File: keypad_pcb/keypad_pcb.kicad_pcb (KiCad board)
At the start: 2 copper layers, 40 x 60 mm, 32 parts

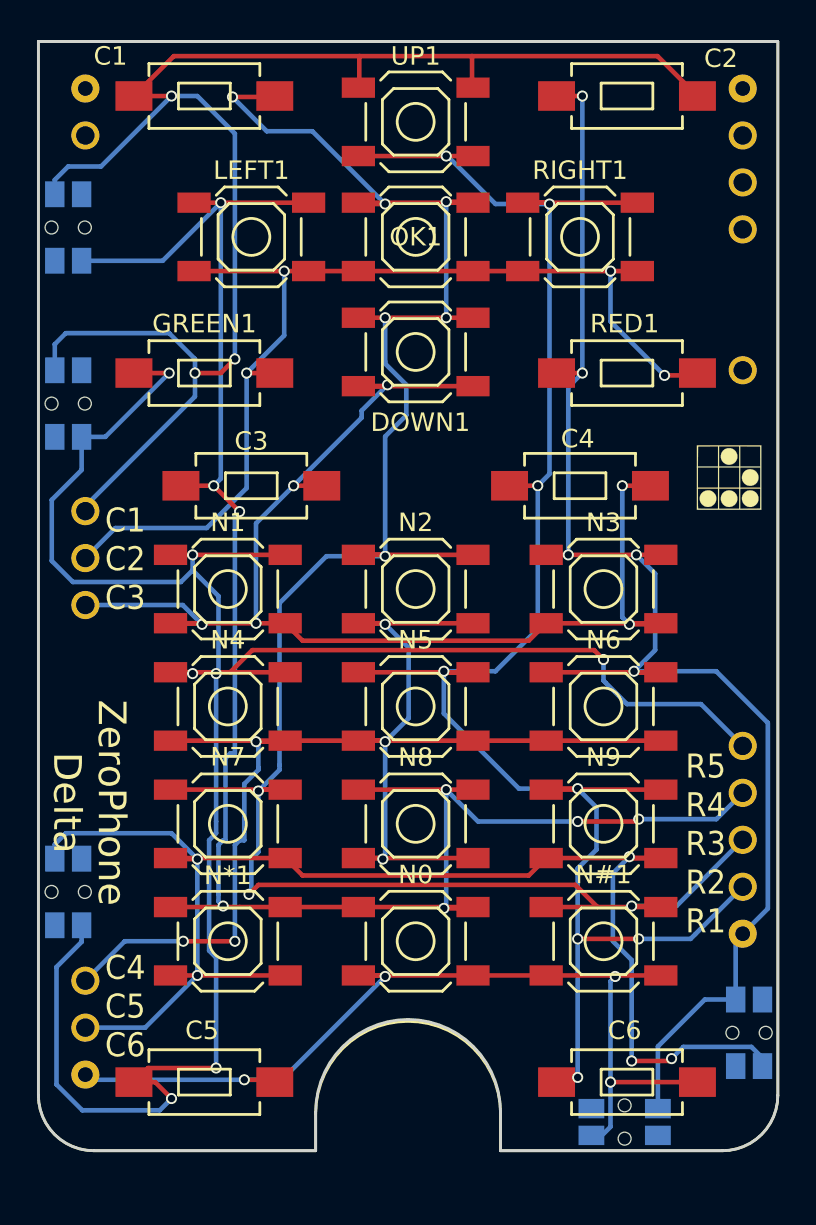
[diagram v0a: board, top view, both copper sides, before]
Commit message: replace keypad footprint on keypad pcb with oval pad version
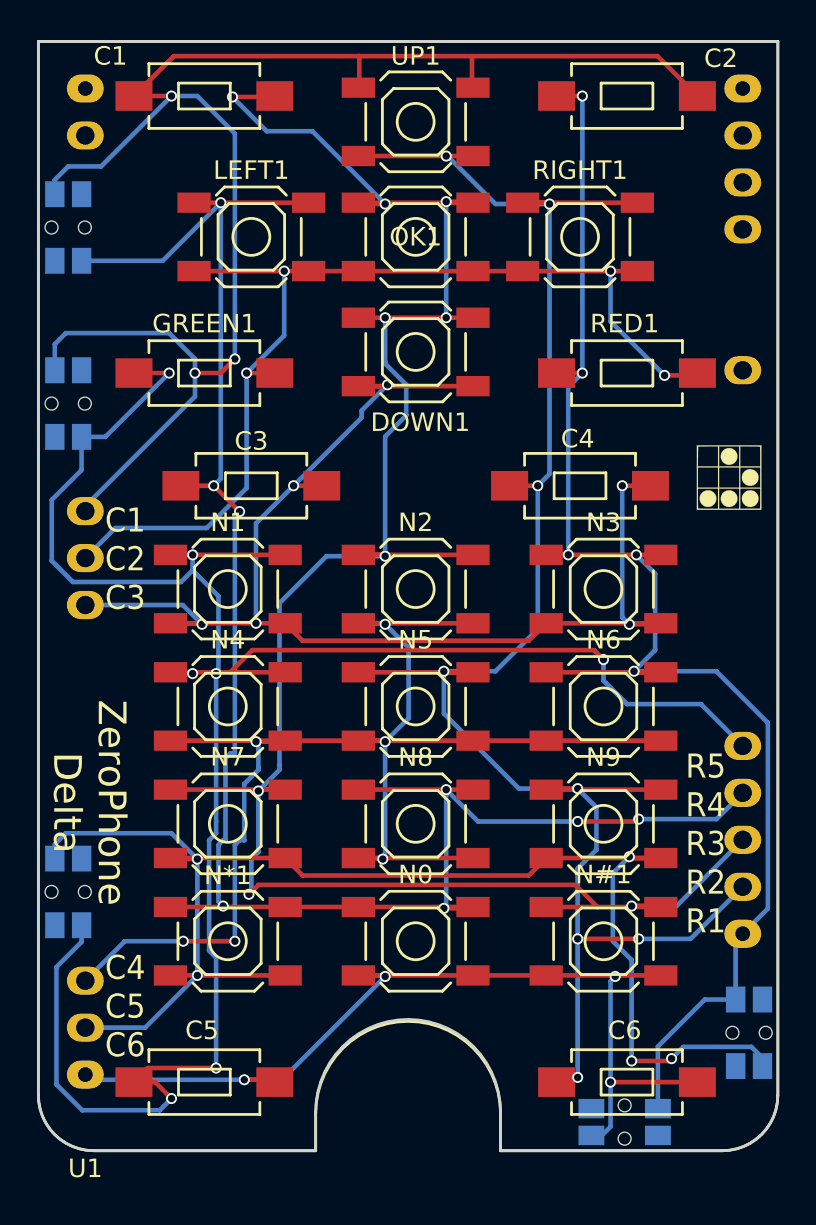
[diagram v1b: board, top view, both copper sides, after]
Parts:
- gave numbers to parts that had none: 1
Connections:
- U1 pad 1: (no net) -> /ROW1
- U1 pad 10: (no net) -> /COL5
- U1 pad 11: (no net) -> /COL6
- U1 pad 12: (no net) -> Net-(U1-Pad12)
- U1 pad 13: (no net) -> Net-(U1-Pad13)
- U1 pad 14: (no net) -> Net-(U1-Pad14)
- U1 pad 15: (no net) -> Net-(U1-Pad15)
- U1 pad 16: (no net) -> Net-(U1-Pad16)
- U1 pad 17: (no net) -> Net-(U1-Pad17)
- U1 pad 18: (no net) -> Net-(U1-Pad18)
- U1 pad 2: (no net) -> /ROW2
- U1 pad 3: (no net) -> /ROW3
- U1 pad 4: (no net) -> /ROW4
- U1 pad 5: (no net) -> /ROW5
- U1 pad 6: (no net) -> /COL1
- U1 pad 7: (no net) -> /COL2
- U1 pad 8: (no net) -> /COL3
- U1 pad 9: (no net) -> /COL4
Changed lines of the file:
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@@
     )
-  )
-  (module common_footprints:keypad_overlay locked (layer F.Cu)
-    (at 148.5011 105.0036)
-    (fp_text reference "" (at 2.54 60.96) (layer F.SilkS)
-      (effects (font (size 1 1) (thickness 0.15)))
-    )
-    (fp_text value KEYPAD_OVERLAY (at 5.08 -2.54) (layer F.Fab)
-      (effects (font (size 1 1) (thickness 0.15)))
-    )
-    (fp_arc (start 37 57) (end 40 57) (angle 90) (layer F.SilkS) (width 0.15))
-    (fp_arc (start 3 57) (end 3 60) (angle 90) (layer F.SilkS) (width 0.15))
-    (fp_arc (start 20 58) (end 15 58) (angle 180) (layer F.SilkS) (width 0.15))
-    (fp_line (start 37 60) (end 25 60) (layer F.SilkS) (width 0.15))
-    (fp_line (start 25 60) (end 25 58) (layer F.SilkS) (width 0.15))
-    (fp_line (start 3 60) (end 15 60) (layer F.SilkS) (width 0.15))
-    (fp_line (start 15 60) (end 15 58) (layer F.SilkS) (width 0.15))
-    (fp_line (start 0 0) (end 0 57) (layer F.SilkS) (width 0.15))
-    (fp_line (start 0 0) (end 40 0) (layer F.SilkS) (width 0.15))
-    (fp_line (start 40 0) (end 40 57) (layer F.SilkS) (width 0.15))
-    (pad 12 thru_hole circle (at 2.54 5.08) (size 1.524 1.524) (drill 1) (layers *.Cu *.Mask))
-    (pad 13 thru_hole circle (at 2.54 2.54) (size 1.524 1.524) (drill 0.8) (layers *.Cu *.Mask))
-    (pad 1 thru_hole circle (at 38.1 48.26) (size 1.524 1.524) (drill 0.8) (layers *.Cu *.Mask))
-    (pad 2 thru_hole circle (at 38.1 45.72) (size 1.524 1.524) (drill 1) (layers *.Cu *.Mask))
-    (pad 3 thru_hole circle (at 38.1 43.18) (size 1.524 1.524) (drill 1) (layers *.Cu *.Mask))
-    (pad 4 thru_hole circle (at 38.1 40.64) (size 1.524 1.524) (drill 1) (layers *.Cu *.Mask))
-    (pad 5 thru_hole circle (at 38.1 38.1) (size 1.524 1.524) (drill 1) (layers *.Cu *.Mask))
-    (pad 6 thru_hole circle (at 2.54 25.4) (size 1.524 1.524) (drill 1) (layers *.Cu *.Mask))
-    (pad 7 thru_hole circle (at 2.54 27.94) (size 1.524 1.524) (drill 1) (layers *.Cu *.Mask))
-    (pad 8 thru_hole circle (at 2.54 30.48) (size 1.524 1.524) (drill 1) (layers *.Cu *.Mask))
-    (pad 9 thru_hole circle (at 2.54 50.8) (size 1.524 1.524) (drill 1) (layers *.Cu *.Mask))
-    (pad 10 thru_hole circle (at 2.54 53.34) (size 1.524 1.524) (drill 1) (layers *.Cu *.Mask))
-    (pad 11 thru_hole circle (at 2.54 55.88) (size 1.524 1.524) (drill 0.8) (layers *.Cu *.Mask))
-    (pad 14 thru_hole circle (at 38.1 2.54) (size 1.524 1.524) (drill 0.8) (layers *.Cu *.Mask))
-    (pad 15 thru_hole circle (at 38.1 5.08) (size 1.524 1.524) (drill 1) (layers *.Cu *.Mask))
-    (pad 16 thru_hole circle (at 38.1 7.62) (size 1.524 1.524) (drill 1) (layers *.Cu *.Mask))
-    (pad 17 thru_hole circle (at 38.1 10.16) (size 1.524 1.524) (drill 1) (layers *.Cu *.Mask))
-    (pad 18 thru_hole circle (at 38.1 17.78) (size 1.524 1.524) (drill 1) (layers *.Cu *.Mask))
   )
   (module art:glider (layer F.Cu)
@@
       (xy -0.112592 -1.580121) (xy -0.048089 -1.591067) (xy 0.077808 -1.587251)) (layer F.SilkS) (width 0.01))
   )
+  (module common_footprints:keypad_overlay locked (layer F.Cu)
+    (at 148.5011 105.0036)
+    (fp_text reference U1 (at 2.54 60.96) (layer F.SilkS)
+      (effects (font (size 1 1) (thickness 0.15)))
+    )
+    (fp_text value KEYPAD_OVERLAY (at 5.08 -2.54) (layer F.Fab)
+      (effects (font (size 1 1) (thickness 0.15)))
+    )
+    (fp_arc (start 37 57) (end 40 57) (angle 90) (layer F.SilkS) (width 0.15))
+    (fp_arc (start 3 57) (end 3 60) (angle 90) (layer F.SilkS) (width 0.15))
+    (fp_arc (start 20 58) (end 15 58) (angle 180) (layer F.SilkS) (width 0.15))
+    (fp_line (start 37 60) (end 25 60) (layer F.SilkS) (width 0.15))
+    (fp_line (start 25 60) (end 25 58) (layer F.SilkS) (width 0.15))
+    (fp_line (start 3 60) (end 15 60) (layer F.SilkS) (width 0.15))
+    (fp_line (start 15 60) (end 15 58) (layer F.SilkS) (width 0.15))
+    (fp_line (start 0 0) (end 0 57) (layer F.SilkS) (width 0.15))
+    (fp_line (start 0 0) (end 40 0) (layer F.SilkS) (width 0.15))
+    (fp_line (start 40 0) (end 40 57) (layer F.SilkS) (width 0.15))
+    (pad 12 thru_hole oval (at 2.54 5.08) (size 2 1.524) (drill 1) (layers *.Cu *.Mask)
+      (net 12 "Net-(U1-Pad12)"))
+    (pad 13 thru_hole oval (at 2.54 2.54) (size 2 1.524) (drill 0.8) (layers *.Cu *.Mask)
+      (net 13 "Net-(U1-Pad13)"))
+    (pad 1 thru_hole oval (at 38.1 48.26) (size 2 1.524) (drill 0.8) (layers *.Cu *.Mask)
+      (net 3 /ROW1))
+    (pad 2 thru_hole oval (at 38.1 45.72) (size 2 1.524) (drill 1) (layers *.Cu *.Mask)
+      (net 6 /ROW2))
+    (pad 3 thru_hole oval (at 38.1 43.18) (size 2 1.524) (drill 1) (layers *.Cu *.Mask)
+      (net 2 /ROW3))
+    (pad 4 thru_hole oval (at 38.1 40.64) (size 2 1.524) (drill 1) (layers *.Cu *.Mask)
+      (net 5 /ROW4))
+    (pad 5 thru_hole oval (at 38.1 38.1) (size 2 1.524) (drill 1) (layers *.Cu *.Mask)
+      (net 8 /ROW5))
+    (pad 6 thru_hole oval (at 2.54 25.4) (size 2 1.524) (drill 1) (layers *.Cu *.Mask)
+      (net 1 /COL1))
+    (pad 7 thru_hole oval (at 2.54 27.94) (size 2 1.524) (drill 1) (layers *.Cu *.Mask)
+      (net 9 /COL2))
+    (pad 8 thru_hole oval (at 2.54 30.48) (size 2 1.524) (drill 1) (layers *.Cu *.Mask)
+      (net 4 /COL3))
+    (pad 9 thru_hole oval (at 2.54 50.8) (size 2 1.524) (drill 1) (layers *.Cu *.Mask)
+      (net 11 /COL4))
+    (pad 10 thru_hole oval (at 2.54 53.34) (size 2 1.524) (drill 1) (layers *.Cu *.Mask)
+      (net 10 /COL5))
+    (pad 11 thru_hole oval (at 2.54 55.88) (size 2 1.524) (drill 0.8) (layers *.Cu *.Mask)
+      (net 7 /COL6))
+    (pad 14 thru_hole oval (at 38.1 2.54) (size 2 1.524) (drill 0.8) (layers *.Cu *.Mask)
+      (net 14 "Net-(U1-Pad14)"))
+    (pad 15 thru_hole oval (at 38.1 5.08) (size 2 1.524) (drill 1) (layers *.Cu *.Mask)
+      (net 15 "Net-(U1-Pad15)"))
+    (pad 16 thru_hole oval (at 38.1 7.62) (size 2 1.524) (drill 1) (layers *.Cu *.Mask)
+      (net 16 "Net-(U1-Pad16)"))
+    (pad 17 thru_hole oval (at 38.1 10.16) (size 2 1.524) (drill 1) (layers *.Cu *.Mask)
+      (net 17 "Net-(U1-Pad17)"))
+    (pad 18 thru_hole oval (at 38.1 17.78) (size 2 1.524) (drill 1) (layers *.Cu *.Mask)
+      (net 18 "Net-(U1-Pad18)"))
+  )
   (gr_line (start 150 112) (end 150 105) (layer B.SilkS) (width 0.2))
